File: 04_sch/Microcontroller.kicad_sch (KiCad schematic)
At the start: 16 parts, among them SW1 SW_Push, SW2 SW_Push, U1 ESP32-WROOM-32

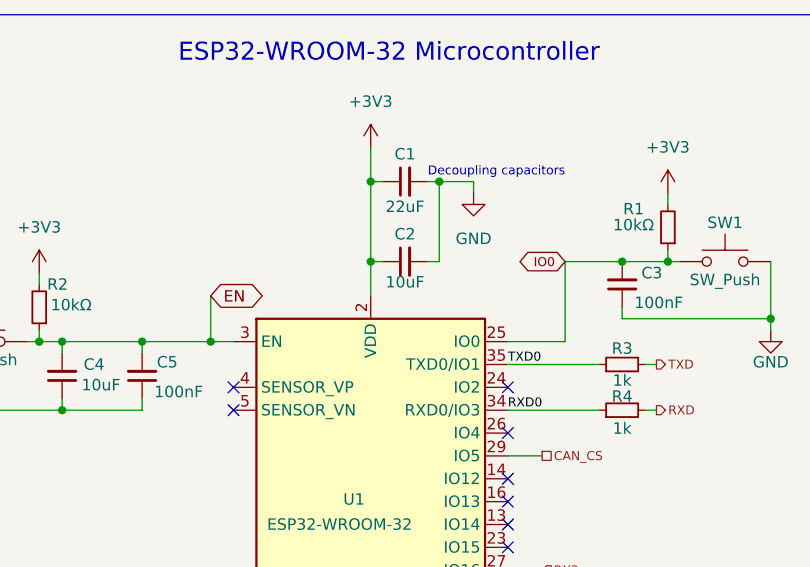
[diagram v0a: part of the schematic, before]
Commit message: Fix tantalum capacitor & JLCPCB codes
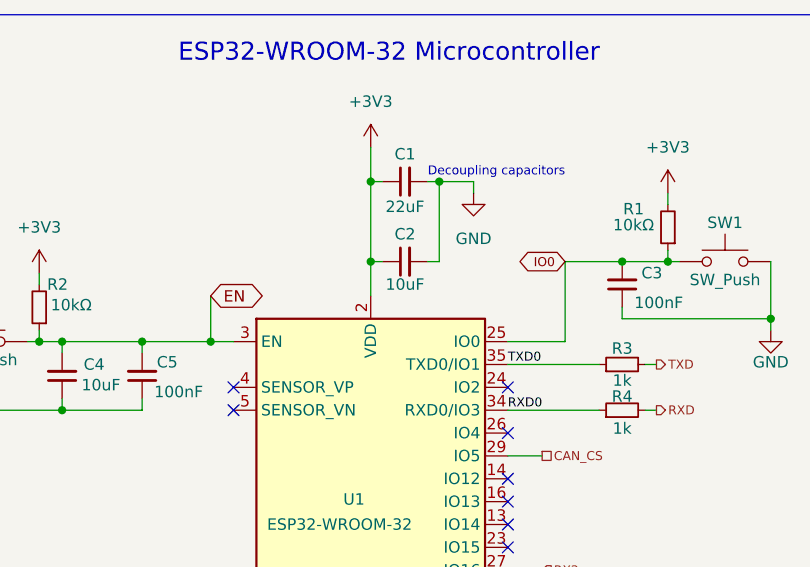
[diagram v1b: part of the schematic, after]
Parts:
- C1: LCSC (none) -> C105484
- C2, C4: LCSC (none) -> C15850
- C3, C5: LCSC (none) -> C49678
- D1: LCSC (none) -> C2296
- D2: LCSC (none) -> C34499
- R1, R2: LCSC (none) -> C191101
- R3, R4: LCSC (none) -> C17513
- R5, R6: LCSC (none) -> C966144
- U1: LCSC (none) -> C82899
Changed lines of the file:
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@@
 			)
 		)
-		(property "LCSC" ""
+		(property "LCSC" "C34499 "
 			(at 181.61 129.54 0)
 			(effects
@@
 			)
 		)
-		(property "LCSC" ""
+		(property "LCSC" "C49678"
 			(at 168.91 73.66 0)
 			(effects
@@
 			)
 		)
-		(property "LCSC" ""
+		(property "LCSC" "C105484"
 			(at 144.78 62.23 0)
 			(effects
@@
 			)
 		)
-		(property "LCSC" ""
+		(property "LCSC" "C49678"
 			(at 115.57 83.82 0)
 			(effects
@@
 			)
 		)
-		(property "LCSC" ""
+		(property "LCSC" "C966144"
 			(at 173.99 119.38 0)
 			(effects
@@
 			)
 		)
-		(property "LCSC" ""
+		(property "LCSC" "C966144"
 			(at 173.99 129.54 0)
 			(effects
@@
 			)
 		)
-		(property "LCSC" ""
+		(property "LCSC" "C82899"
 			(at 140.97 110.49 0)
 			(effects
@@
 			)
 		)
-		(property "LCSC" ""
+		(property "LCSC" "C191101"
 			(at 173.99 67.31 0)
 			(effects
@@
 			)
 		)
-		(property "LCSC" ""
+		(property "LCSC" "C15850"
 			(at 106.68 83.82 0)
 			(effects
@@
 			)
 		)
-		(property "LCSC" ""
+		(property "LCSC" "C191101"
 			(at 104.14 76.2 0)
 			(effects
@@
 			)
 		)
-		(property "LCSC" ""
+		(property "LCSC" "C17513"
 			(at 168.91 87.63 0)
 			(effects
@@
 		)
 		(property "Value" "10uF"
-			(at 144.78 73.406 90)
+			(at 144.78 73.66 90)
 			(effects
 				(font
@@
 			)
 		)
-		(property "LCSC" ""
+		(property "LCSC" "C15850"
 			(at 144.78 71.12 0)
 			(effects
@@
 			)
 		)
-		(property "LCSC" ""
+		(property "LCSC" "C17513"
 			(at 168.91 82.55 0)
 			(effects
@@
 			)
 		)
-		(property "LCSC" ""
+		(property "LCSC" "C2296"
 			(at 181.61 119.38 0)
 			(effects

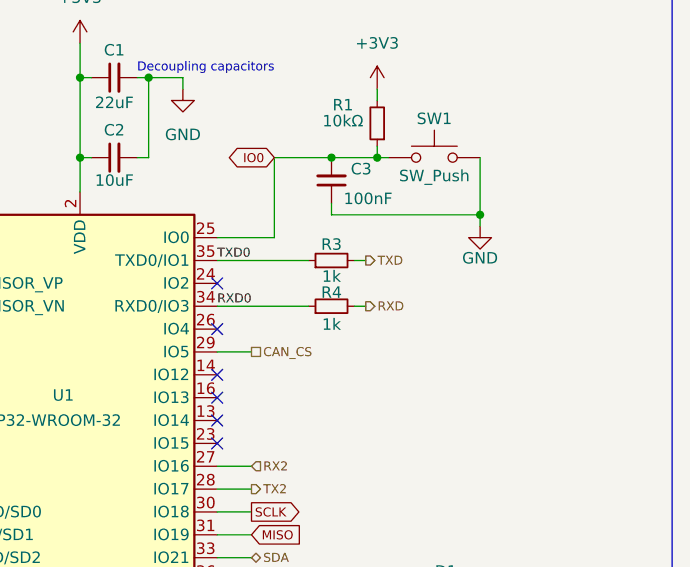
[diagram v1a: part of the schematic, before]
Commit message: Fix CP2102 connection
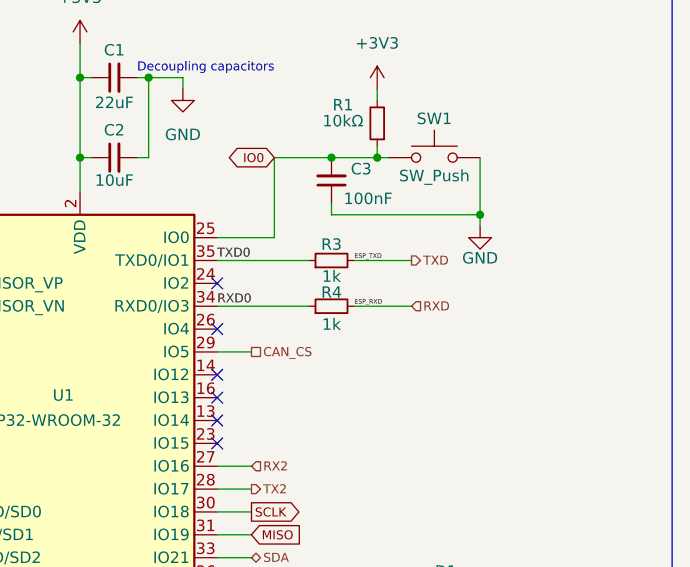
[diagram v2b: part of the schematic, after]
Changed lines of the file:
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@@
 	(wire
 		(pts
-			(xy 172.72 87.63) (xy 171.45 87.63)
+			(xy 177.8 87.63) (xy 171.45 87.63)
 		)
 		(stroke
@@
 	(wire
 		(pts
-			(xy 172.72 82.55) (xy 171.45 82.55)
+			(xy 177.8 82.55) (xy 171.45 82.55)
 		)
 		(stroke
@@
 			(font
 				(size 1 1)
+			)
+			(justify left bottom)
+		)
+	)
+	(label "ESP_RXD"
+		(at 171.45 87.63 0)
+		(fields_autoplaced yes)
+		(effects
+			(font
+				(size 0.5 0.5)
+			)
+			(justify left bottom)
+		)
+	)
+	(label "ESP_TXD"
+		(at 171.45 82.55 0)
+		(fields_autoplaced yes)
+		(effects
+			(font
+				(size 0.5 0.5)
 			)
 			(justify left bottom)
@@
 	)
 	(hierarchical_label "RXD"
-		(shape output)
-		(at 172.72 87.63 0)
+		(shape input)
+		(at 177.8 87.63 0)
 		(fields_autoplaced yes)
 		(effects
@@
 	(hierarchical_label "TXD"
 		(shape output)
-		(at 172.72 82.55 0)
-		(fields_autoplaced yes)
-		(effects
+		(at 177.8 82.55 0)
+		(fields_autoplaced yes)
+		(effects

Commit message: Update 01_Specs and Gerber
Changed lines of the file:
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@@
-		)
-	)
-	(label "ESP_RXD"
-		(at 171.45 87.63 0)
-		(fields_autoplaced yes)
-		(effects
-			(font
-				(size 0.5 0.5)
-			)
-			(justify left bottom)
-		)
-	)
-	(label "ESP_TXD"
-		(at 171.45 82.55 0)
-		(fields_autoplaced yes)
-		(effects
-			(font
-				(size 0.5 0.5)
-			)
-			(justify left bottom)
 		)
 	)
